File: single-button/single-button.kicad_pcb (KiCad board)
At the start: 2 copper layers, 24.5 x 15 mm, 5 parts, among them SW1 SW_Push_DPDT

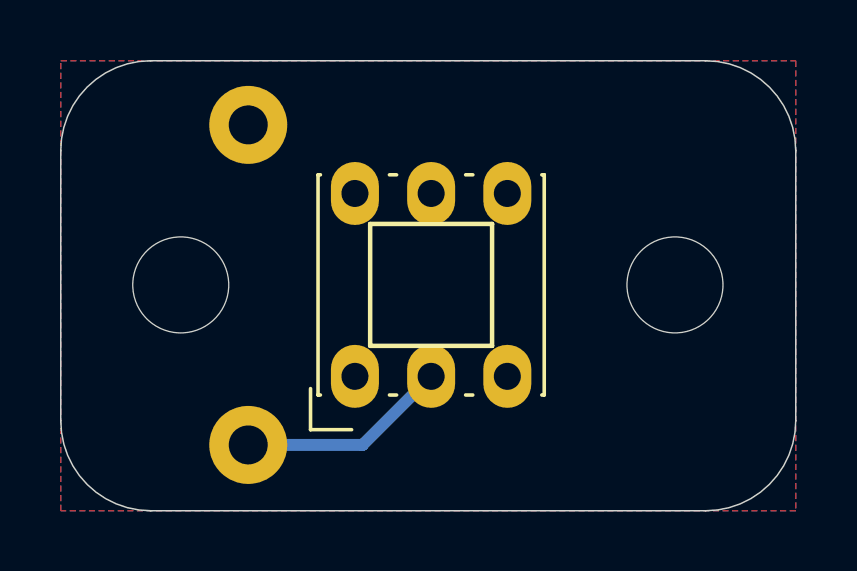
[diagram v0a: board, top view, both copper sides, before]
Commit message: Single-button: add pads to other side to make mounting easier.
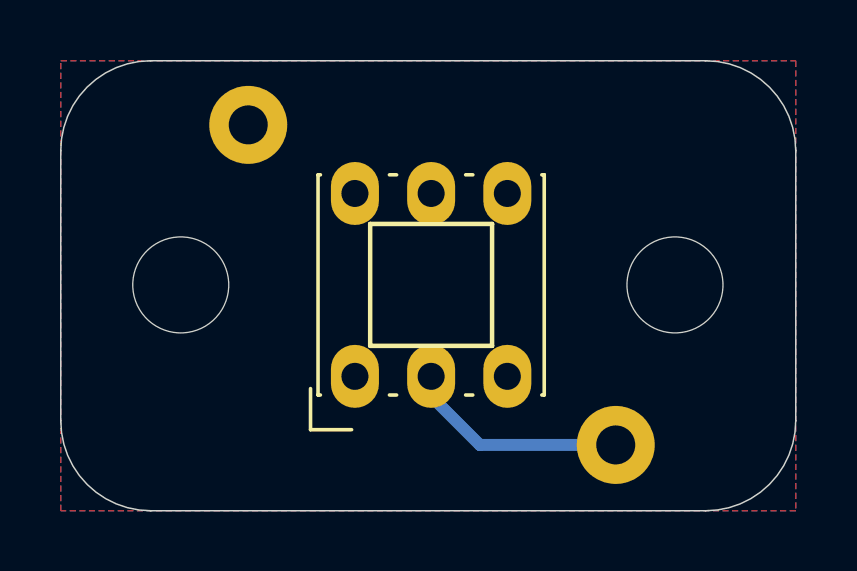
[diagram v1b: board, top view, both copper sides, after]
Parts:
- moved CSIG1 12.2 mm to (107.5, 35.3)
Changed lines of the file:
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@@
     (thickness 1.6)
     (drawings 546)
-    (tracks 2)
+    (tracks 3)
     (zones 0)
     (modules 5)
@@
     (add_net GND)
     (add_net "Net-(CSIG1-Pad1)")
-    (add_net "Net-(SW1-Pad1)")
-    (add_net "Net-(SW1-Pad4)")
-    (add_net "Net-(SW1-Pad5)")
-    (add_net "Net-(SW1-Pad6)")
   )
   (module Connector_Pin:Pin_D1.3mm_L11.0mm (layer B.Cu)
@@
       (effects (font (size 1 1) (thickness 0.15)) (justify mirror))
     )
+    (fp_circle (center 0 0) (end 1.6 -0.05) (layer B.SilkS) (width 0.12))
+    (fp_circle (center 0 0) (end 1.25 0.05) (layer B.Fab) (width 0.12))
+    (fp_circle (center 0 0) (end 0.65 0.05) (layer B.Fab) (width 0.12))
+    (fp_circle (center 0 0) (end 1.8 0) (layer B.CrtYd) (width 0.05))
     (fp_text user %R (at 0 -2.4) (layer B.Fab)
       (effects (font (size 1 1) (thickness 0.15)) (justify mirror))
     )
-    (fp_circle (center 0 0) (end 1.8 0) (layer B.CrtYd) (width 0.05))
-    (fp_circle (center 0 0) (end 0.65 0.05) (layer B.Fab) (width 0.12))
-    (fp_circle (center 0 0) (end 1.25 0.05) (layer B.Fab) (width 0.12))
-    (fp_circle (center 0 0) (end 1.6 -0.05) (layer B.SilkS) (width 0.12))
     (pad 1 thru_hole circle (at 0 0) (size 2.6 2.6) (drill 1.3) (layers *.Cu *.Mask)
       (net 1 GND))
@@
       (effects (font (size 1 1) (thickness 0.15)))
     )
+    (fp_line (start 2.032 -2.032) (end -2.032 -2.032) (layer F.SilkS) (width 0.15))
+    (fp_line (start 2.032 2.032) (end 2.032 -2.032) (layer F.SilkS) (width 0.15))
+    (fp_line (start -2.032 2.032) (end 2.032 2.032) (layer F.SilkS) (width 0.15))
+    (fp_line (start -2.032 -2.032) (end -2.032 2.032) (layer F.SilkS) (width 0.15))
+    (fp_line (start -4.572 -3.9) (end -4.572 3.9) (layer F.CrtYd) (width 0.05))
+    (fp_line (start -3.55 3.65) (end -3.55 -3.556) (layer F.Fab) (width 0.1))
+    (fp_line (start 4.572 3.9) (end 4.572 -3.9) (layer F.CrtYd) (width 0.05))
+    (fp_line (start 3.55 -3.65) (end 3.55 3.65) (layer F.Fab) (width 0.1))
+    (fp_line (start 3.55 3.65) (end -3.55 3.65) (layer F.Fab) (width 0.1))
+    (fp_line (start -4.572 3.9) (end 4.572 3.9) (layer F.CrtYd) (width 0.05))
+    (fp_line (start -4.826 -2.65) (end -4.826 -4.02) (layer F.SilkS) (width 0.12))
+    (fp_line (start 3.67 1.15) (end 3.67 1.39) (layer F.SilkS) (width 0.12))
+    (fp_line (start -3.67 -3.69) (end -3.67 -3.77) (layer F.SilkS) (width 0.12))
+    (fp_line (start -3.67 -3.77) (end 3.67 -3.77) (layer F.SilkS) (width 0.12))
+    (fp_line (start 3.67 -1.39) (end 3.67 -1.15) (layer F.SilkS) (width 0.12))
+    (fp_line (start 3.67 3.77) (end 3.67 3.69) (layer F.SilkS) (width 0.12))
+    (fp_line (start -3.67 -1.39) (end -3.67 -1.15) (layer F.SilkS) (width 0.12))
+    (fp_line (start -3.67 3.69) (end -3.67 3.77) (layer F.SilkS) (width 0.12))
+    (fp_line (start -3.556 -3.65) (end 3.55 -3.65) (layer F.Fab) (width 0.1))
+    (fp_line (start 3.67 -3.77) (end 3.67 -3.69) (layer F.SilkS) (width 0.12))
+    (fp_line (start -4.826 -4.02) (end -3.456 -4.02) (layer F.SilkS) (width 0.12))
+    (fp_line (start -3.67 1.15) (end -3.67 1.39) (layer F.SilkS) (width 0.12))
+    (fp_line (start -3.67 3.77) (end 3.67 3.77) (layer F.SilkS) (width 0.12))
     (fp_line (start 4.572 -3.9) (end -4.572 -3.9) (layer F.CrtYd) (width 0.05))
-    (fp_line (start -3.67 3.77) (end 3.67 3.77) (layer F.SilkS) (width 0.12))
-    (fp_line (start -3.67 1.15) (end -3.67 1.39) (layer F.SilkS) (width 0.12))
-    (fp_line (start -4.826 -4.02) (end -3.456 -4.02) (layer F.SilkS) (width 0.12))
-    (fp_line (start 3.67 -3.77) (end 3.67 -3.69) (layer F.SilkS) (width 0.12))
-    (fp_line (start -3.556 -3.65) (end 3.55 -3.65) (layer F.Fab) (width 0.1))
-    (fp_line (start -3.67 3.69) (end -3.67 3.77) (layer F.SilkS) (width 0.12))
-    (fp_line (start -3.67 -1.39) (end -3.67 -1.15) (layer F.SilkS) (width 0.12))
-    (fp_line (start 3.67 3.77) (end 3.67 3.69) (layer F.SilkS) (width 0.12))
-    (fp_line (start 3.67 -1.39) (end 3.67 -1.15) (layer F.SilkS) (width 0.12))
-    (fp_line (start -3.67 -3.77) (end 3.67 -3.77) (layer F.SilkS) (width 0.12))
-    (fp_line (start -3.67 -3.69) (end -3.67 -3.77) (layer F.SilkS) (width 0.12))
-    (fp_line (start 3.67 1.15) (end 3.67 1.39) (layer F.SilkS) (width 0.12))
-    (fp_line (start -4.826 -2.65) (end -4.826 -4.02) (layer F.SilkS) (width 0.12))
-    (fp_line (start -4.572 3.9) (end 4.572 3.9) (layer F.CrtYd) (width 0.05))
-    (fp_line (start 3.55 3.65) (end -3.55 3.65) (layer F.Fab) (width 0.1))
-    (fp_line (start 3.55 -3.65) (end 3.55 3.65) (layer F.Fab) (width 0.1))
-    (fp_line (start 4.572 3.9) (end 4.572 -3.9) (layer F.CrtYd) (width 0.05))
-    (fp_line (start -3.55 3.65) (end -3.55 -3.556) (layer F.Fab) (width 0.1))
-    (fp_line (start -4.572 -3.9) (end -4.572 3.9) (layer F.CrtYd) (width 0.05))
-    (fp_line (start -2.032 -2.032) (end -2.032 2.032) (layer F.SilkS) (width 0.15))
-    (fp_line (start -2.032 2.032) (end 2.032 2.032) (layer F.SilkS) (width 0.15))
-    (fp_line (start 2.032 2.032) (end 2.032 -2.032) (layer F.SilkS) (width 0.15))
-    (fp_line (start 2.032 -2.032) (end -2.032 -2.032) (layer F.SilkS) (width 0.15))
     (pad 6 thru_hole oval (at 3.048 0 90) (size 2.1 1.6) (drill 0.9) (layers *.Cu *.Mask))
     (pad 4 thru_hole oval (at 3.048 2.54 90) (size 2.1 1.6) (drill 0.9) (layers *.Cu *.Mask))
@@
       (effects (font (size 1 1) (thickness 0.15)))
     )
+    (fp_circle (center 0 0) (end 3.45 0) (layer F.CrtYd) (width 0.05))
     (fp_circle (center 0 0) (end 3.2 0) (layer Cmts.User) (width 0.15))
-    (fp_circle (center 0 0) (end 3.45 0) (layer F.CrtYd) (width 0.05))
     (fp_text user %R (at 0.3 0) (layer F.Fab)
       (effects (font (size 1 1) (thickness 0.15)))
@@
       (effects (font (size 1 1) (thickness 0.15)))
     )
+    (fp_circle (center 0 0) (end 3.45 0) (layer F.CrtYd) (width 0.05))
     (fp_circle (center 0 0) (end 3.2 0) (layer Cmts.User) (width 0.15))
-    (fp_circle (center 0 0) (end 3.45 0) (layer F.CrtYd) (width 0.05))
     (fp_text user %R (at 0.3 0 90) (layer F.Fab)
       (effects (font (size 1 1) (thickness 0.15)))
@@
   )
   (module Connector_Pin:Pin_D1.3mm_L11.0mm (layer B.Cu)
-    (at 95.25 35.306)
+    (at 107.5 35.306)
     (descr "solder Pin_ diameter 1.3mm, hole diameter 1.3mm, length 11.0mm")
     (tags "solder Pin_ pressfit")
@@
       (effects (font (size 1 1) (thickness 0.15)) (justify mirror))
     )
+    (fp_circle (center 0 0) (end 1.6 -0.05) (layer B.SilkS) (width 0.12))
+    (fp_circle (center 0 0) (end 1.25 0.05) (layer B.Fab) (width 0.12))
+    (fp_circle (center 0 0) (end 0.65 0.05) (layer B.Fab) (width 0.12))
     (fp_circle (center 0 0) (end 1.8 0) (layer B.CrtYd) (width 0.05))
-    (fp_circle (center 0 0) (end 0.65 0.05) (layer B.Fab) (width 0.12))
-    (fp_circle (center 0 0) (end 1.25 0.05) (layer B.Fab) (width 0.12))
-    (fp_circle (center 0 0) (end 1.6 -0.05) (layer B.SilkS) (width 0.12))
     (fp_text user %R (at 0 -2.4) (layer B.Fab)
       (effects (font (size 1 1) (thickness 0.15)) (justify mirror))
@@
   (gr_arc (start 110.5 25.5) (end 113.5 25.5) (angle -90) (layer Edge.Cuts) (width 0.05))
   (gr_arc (start 92 25.5) (end 92 22.5) (angle -90) (layer Edge.Cuts) (width 0.05))
-  (segment (start 99.06 35.306) (end 101.346 33.02) (width 0.4) (layer B.Cu) (net 2))
-  (segment (start 95.25 35.306) (end 99.06 35.306) (width 0.4) (layer B.Cu) (net 2))
+  (segment (start 101.346 33.683) (end 101.346 33.02) (width 0.4) (layer B.Cu) (net 2))
+  (segment (start 102.969 35.306) (end 101.346 33.683) (width 0.4) (layer B.Cu) (net 2))
+  (segment (start 107.5 35.306) (end 102.969 35.306) (width 0.4) (layer B.Cu) (net 2))
   (zone (net 1) (net_name GND) (layer B.Cu) (hatch edge 0.508)
     (connect_pads (clearance 0.4))
